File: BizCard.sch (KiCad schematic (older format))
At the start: 4 parts

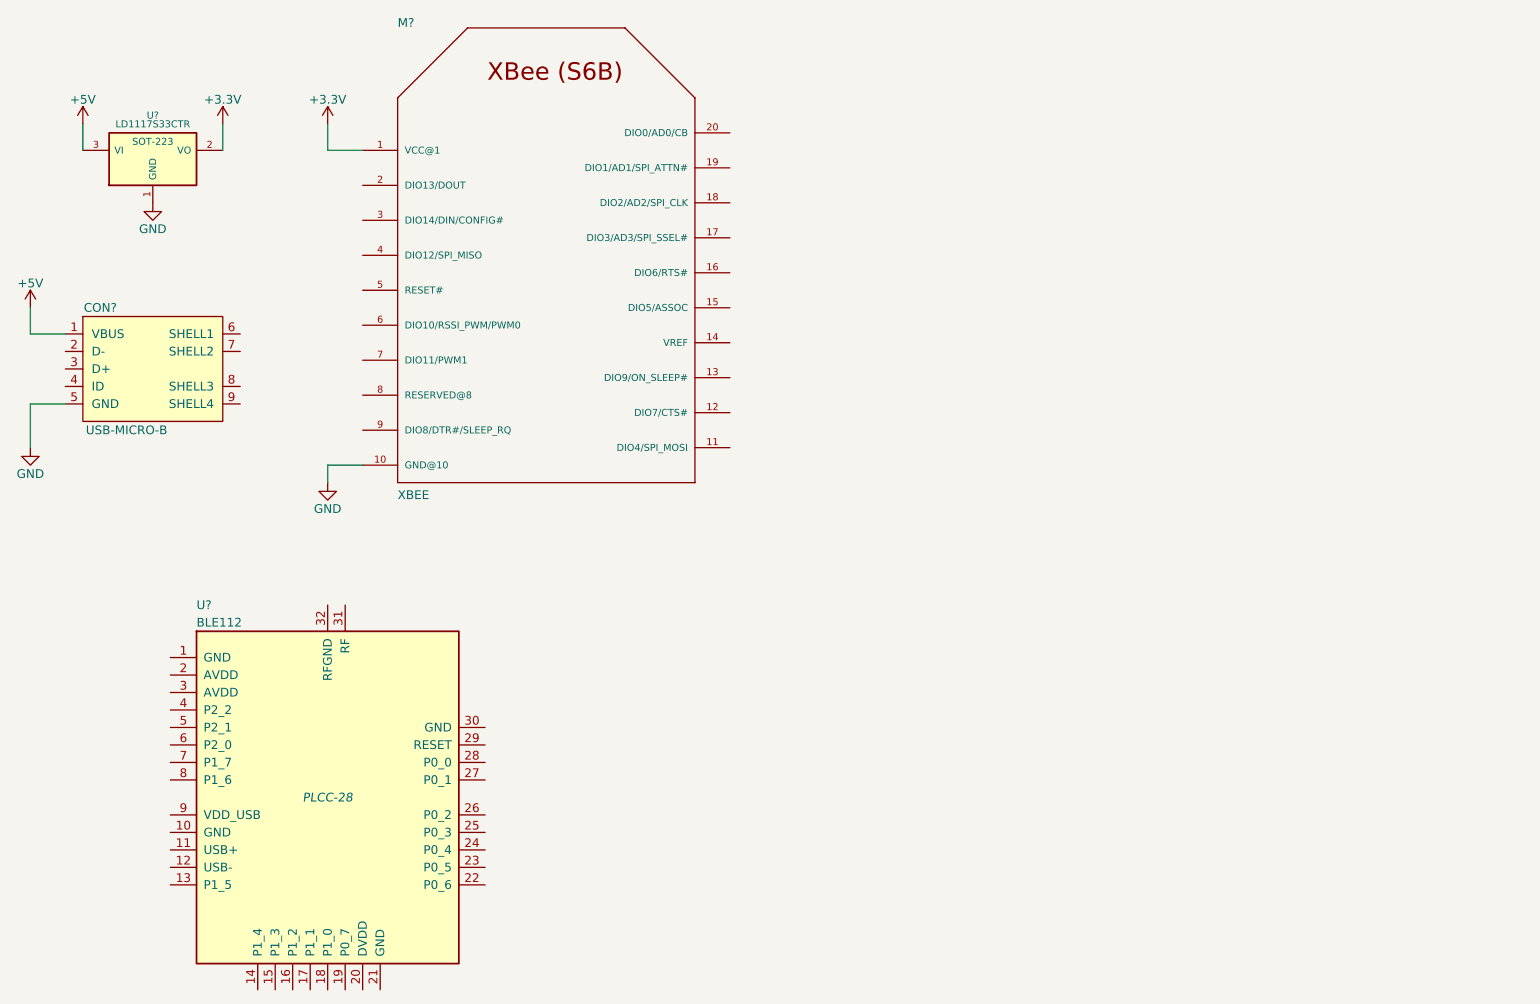
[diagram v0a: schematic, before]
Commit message: Removed Bluetooth, added connectors to XBee
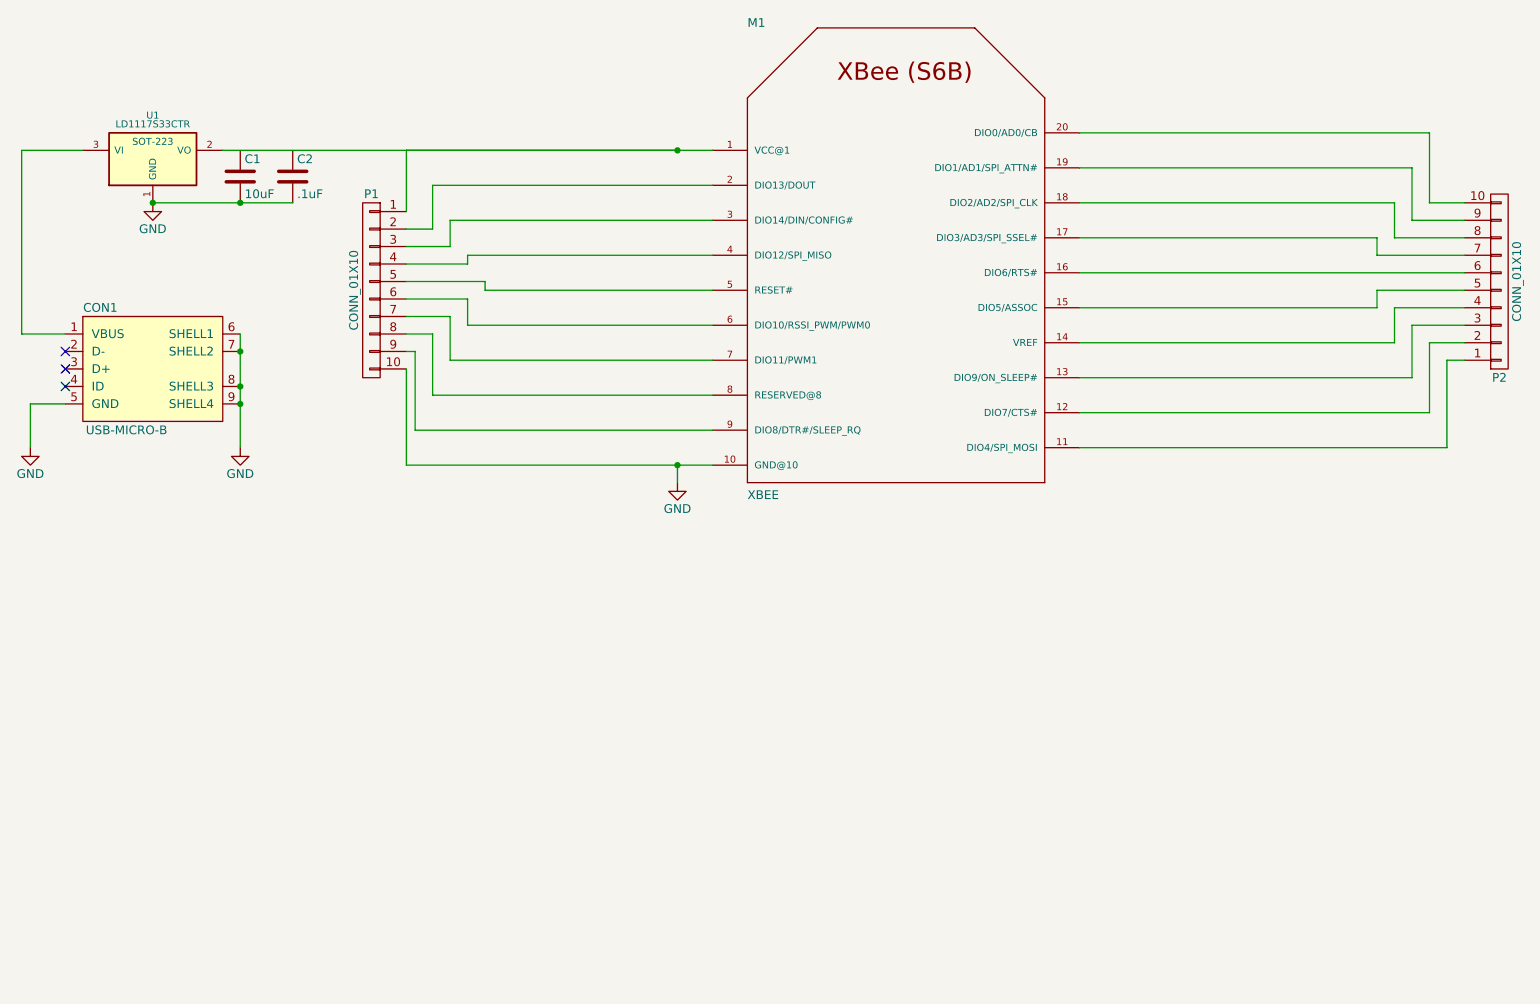
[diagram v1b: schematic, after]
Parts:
- removed U?: BLE112, PLCC-28, symbol BLE112
- added C1: 10uF, symbol C
- added C2: .1uF, symbol C
- added P1, P2: CONN_01X10, symbol CONN_01X10
- gave numbers to parts that had none: 3
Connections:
- net GND: now also CON1.6 (SHELL1), CON1.7 (SHELL2), CON1.8 (SHELL3), CON1.9 (SHELL4), C1.2, C2.2, P1.10 (P10)
- net at M1.11 (DIO4/SPI_MOSI): now also P2.1 (P1)
- net at M1.12 (DIO7/CTS#): now also P2.2 (P2)
- net at M1.13 (DIO9/ON_SLEEP#): now also P2.3 (P3)
- net at M1.14 (VREF): now also P2.4 (P4)
- net at M1.15 (DIO5/ASSOC): now also P2.5 (P5)
- net at M1.16 (DIO6/RTS#): now also P2.6 (P6)
- net at M1.17 (DIO3/AD3/SPI_SSEL#): now also P2.7 (P7)
- net at M1.18 (DIO2/AD2/SPI_CLK): now also P2.8 (P8)
- net at M1.19 (DIO1/AD1/SPI_ATTN#): now also P2.9 (P9)
- net at M1.2 (DIO13/DOUT): now also P1.2 (P2)
- net at M1.20 (DIO0/AD0/CB): now also P2.10 (P10)
- net at M1.3 (DIO14/DIN/CONFIG#): now also P1.3 (P3)
- net at M1.4 (DIO12/SPI_MISO): now also P1.4 (P4)
- net at M1.5 (RESET#): now also P1.5 (P5)
- net at M1.6 (DIO10/RSSI_PWM/PWM0): now also P1.6 (P6)
- net at M1.7 (DIO11/PWM1): now also P1.7 (P7)
- net at M1.8 (RESERVED@8): now also P1.8 (P8)
- net at M1.9 (DIO8/DTR#/SLEEP_RQ): now also P1.9 (P9)
- net +3V3: no longer names the net of M1.1 (VCC@1), U1.2 (VO)
- net +3V3: now also P1.1 (P1)
- net +5V: no longer names the net of CON1.1 (VBUS), U1.3 (VI)
- no-connect marks 0 -> 3
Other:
- moved on the sheet: M1
